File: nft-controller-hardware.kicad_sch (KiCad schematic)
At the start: 24 parts, among them J0 Micro_SD_Card_Det, U0 DS3231M, U1 ADS1115IDGS

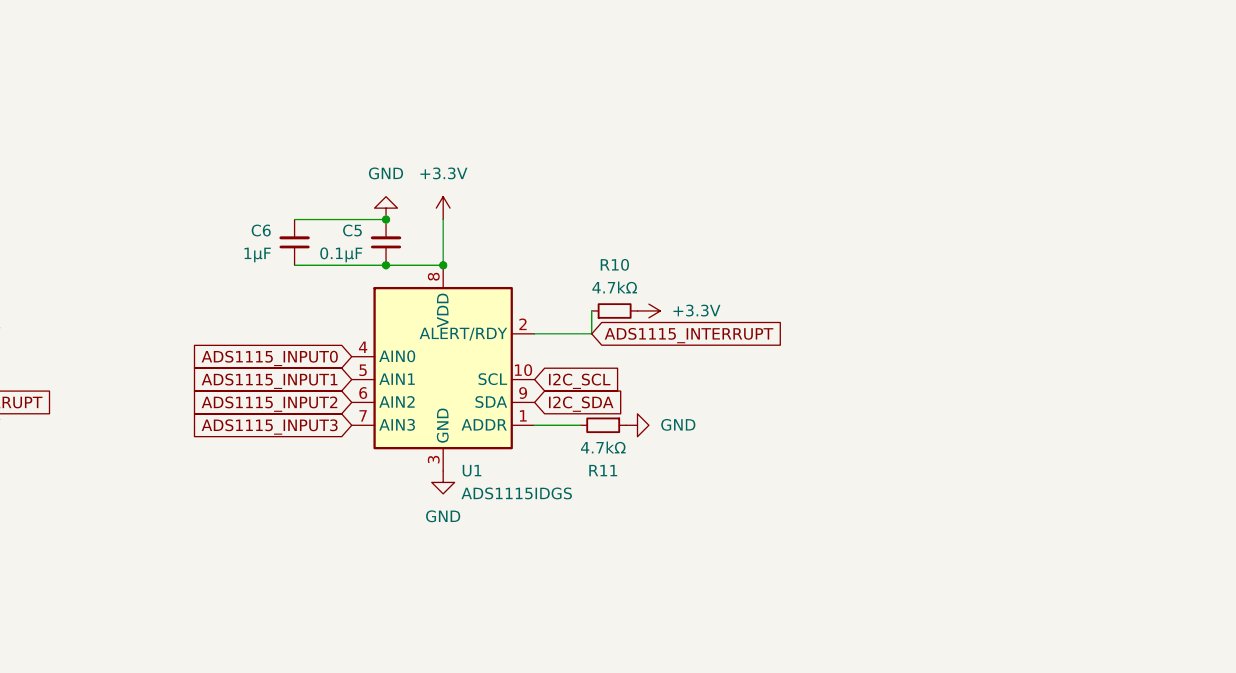
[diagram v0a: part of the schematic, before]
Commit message: Add ADC connectors to the memory expansion board.
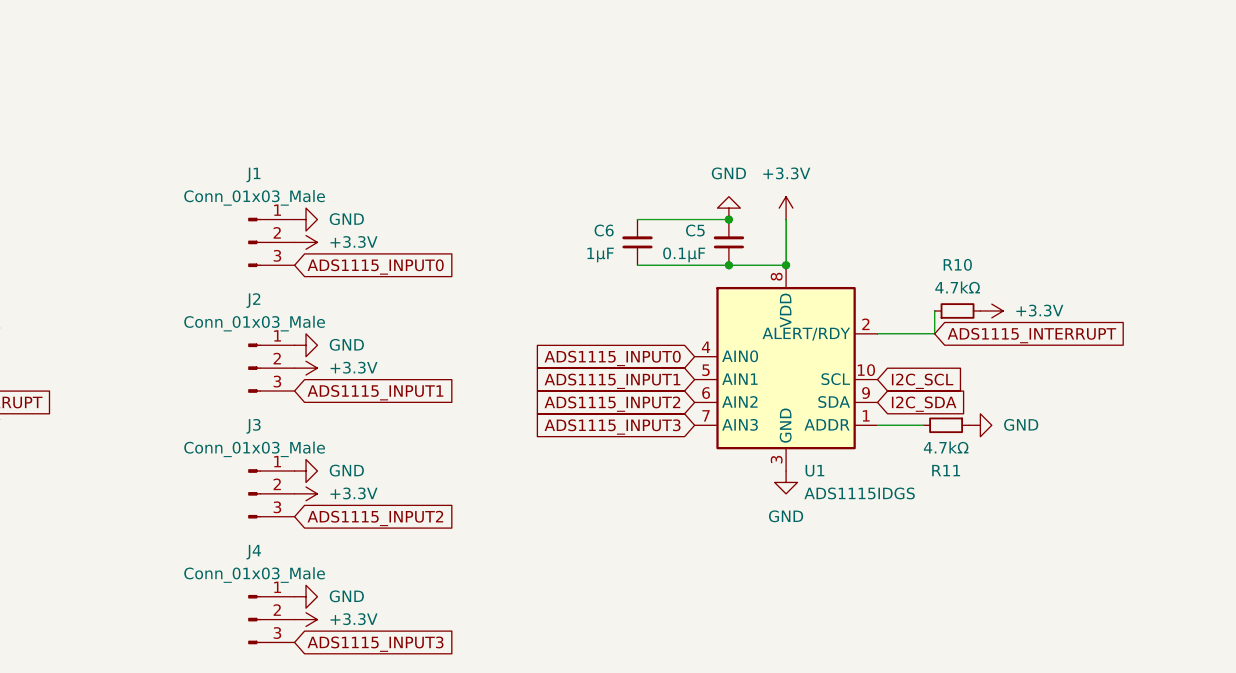
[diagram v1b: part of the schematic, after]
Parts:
- added J1, J2, J3, J4: Conn_01x03_Male, Connector_JST:JST_SH_SM03B-SRSS-TB_1x03-1MP_P1.00mm_Horizontal, symbol Connector:Conn_01x03_Male
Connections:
- net +3V3: now also J1.2 (Pin_2), J2.2 (Pin_2), J3.2 (Pin_2), J4.2 (Pin_2)
- net ADS1115_INPUT0: now also J1.3 (Pin_3)
- net ADS1115_INPUT1: now also J2.3 (Pin_3)
- net ADS1115_INPUT2: now also J3.3 (Pin_3)
- net ADS1115_INPUT3: now also J4.3 (Pin_3)
- net GND: now also J1.1 (Pin_1), J2.1 (Pin_1), J3.1 (Pin_1), J4.1 (Pin_1)
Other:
- moved on the sheet: C5, C6, R10, R11, U1

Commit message: Size all SMD capacitors to 2012.
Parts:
- C0, C1, C2, C3, C4, C5, C6: footprint (none) -> Capacitor_SMD:C_0805_2012Metric
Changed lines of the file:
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@@
       (effects (font (size 1.27 1.27)) (justify right))
     )
-    (property "Footprint" "" (id 2) (at 144.78 124.46 0)
+    (property "Footprint" "Capacitor_SMD:C_0805_2012Metric" (id 2) (at 144.78 124.46 0)
       (effects (font (size 1.27 1.27)) hide)
     )
@@
     (property "Reference" "C2" (id 0) (at 114.2937 67.31 90))
     (property "Value" "1μF" (id 1) (at 114.2937 64.77 90))
-    (property "Footprint" "" (id 2) (at 114.3 60.96 0)
+    (property "Footprint" "Capacitor_SMD:C_0805_2012Metric" (id 2) (at 114.3 60.96 0)
       (effects (font (size 1.27 1.27)) hide)
     )
@@
       (effects (font (size 1.27 1.27)) (justify right))
     )
-    (property "Footprint" "" (id 2) (at 45.72 27.94 0)
+    (property "Footprint" "Capacitor_SMD:C_0805_2012Metric" (id 2) (at 45.72 27.94 0)
       (effects (font (size 1.27 1.27)) hide)
     )
@@
       (effects (font (size 1.27 1.27)) (justify right))
     )
-    (property "Footprint" "" (id 2) (at 154.94 124.46 0)
+    (property "Footprint" "Capacitor_SMD:C_0805_2012Metric" (id 2) (at 154.94 124.46 0)
       (effects (font (size 1.27 1.27)) hide)
     )
@@
       (effects (font (size 1.27 1.27)) (justify left))
     )
-    (property "Footprint" "" (id 2) (at 35.56 127 0)
+    (property "Footprint" "Capacitor_SMD:C_0805_2012Metric" (id 2) (at 35.56 127 0)
       (effects (font (size 1.27 1.27)) hide)
     )
@@
     (property "Reference" "C1" (id 0) (at 114.2937 57.15 90))
     (property "Value" "0.1μF" (id 1) (at 114.2937 54.61 90))
-    (property "Footprint" "" (id 2) (at 114.3 50.8 0)
+    (property "Footprint" "Capacitor_SMD:C_0805_2012Metric" (id 2) (at 114.3 50.8 0)
       (effects (font (size 1.27 1.27)) hide)
     )
@@
       (effects (font (size 1.27 1.27)) (justify left))
     )
-    (property "Footprint" "" (id 2) (at 25.4 127 0)
+    (property "Footprint" "Capacitor_SMD:C_0805_2012Metric" (id 2) (at 25.4 127 0)
       (effects (font (size 1.27 1.27)) hide)
     )
@@
     )
     (path "/2d1d279f-dfe4-4ca3-b77e-718d321d7994"
-      (reference "C0") (unit 1) (value "10μF") (footprint "")
+      (reference "C0") (unit 1) (value "10μF") (footprint "Capacitor_SMD:C_0805_2012Metric")
     )
     (path "/eeddbc36-f79b-450c-949d-4075e2ee2f66"
-      (reference "C1") (unit 1) (value "0.1μF") (footprint "")
+      (reference "C1") (unit 1) (value "0.1μF") (footprint "Capacitor_SMD:C_0805_2012Metric")
     )
     (path "/24f11e55-c826-4157-a61d-34245686f7ab"
-      (reference "C2") (unit 1) (value "1μF") (footprint "")
+      (reference "C2") (unit 1) (value "1μF") (footprint "Capacitor_SMD:C_0805_2012Metric")
     )
     (path "/d8c4663a-d59c-454a-82f0-37282ddac6f7"
-      (reference "C3") (unit 1) (value "0.1μF") (footprint "")
+      (reference "C3") (unit 1) (value "0.1μF") (footprint "Capacitor_SMD:C_0805_2012Metric")
     )
     (path "/f49fb1be-539b-44b6-83f7-76b29af6c384"
-      (reference "C4") (unit 1) (value "1μF") (footprint "")
+      (reference "C4") (unit 1) (value "1μF") (footprint "Capacitor_SMD:C_0805_2012Metric")
     )
     (path "/5a402334-f447-450e-a114-56a61e72962d"
-      (reference "C5") (unit 1) (value "0.1μF") (footprint "")
+      (reference "C5") (unit 1) (value "0.1μF") (footprint "Capacitor_SMD:C_0805_2012Metric")
     )
     (path "/02bbd9ce-68b0-4271-9eb1-4b98656ac324"
-      (reference "C6") (unit 1) (value "1μF") (footprint "")
+      (reference "C6") (unit 1) (value "1μF") (footprint "Capacitor_SMD:C_0805_2012Metric")
     )
     (path "/178ea558-ba01-4660-95f1-80290a5a4f0c"

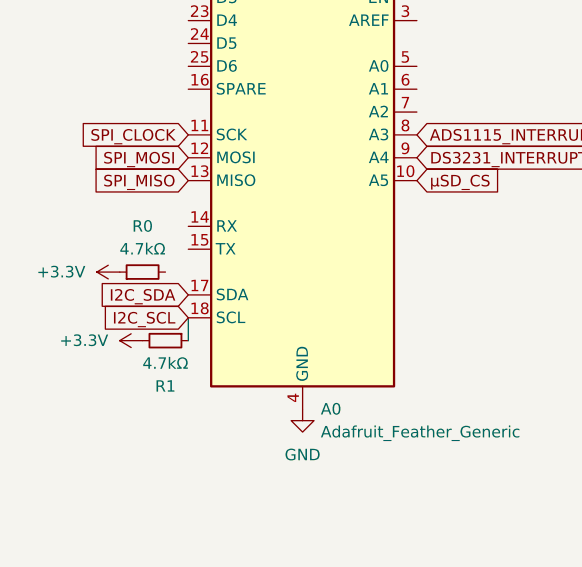
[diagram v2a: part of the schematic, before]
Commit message: Fix a missing connection to an I2C SDA pull-up resistor.
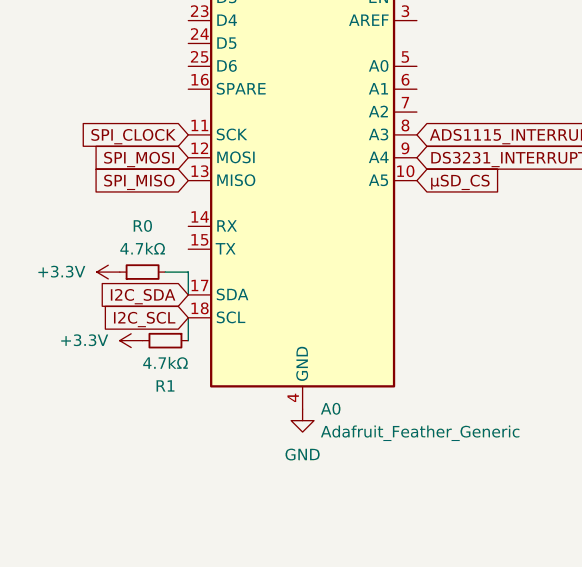
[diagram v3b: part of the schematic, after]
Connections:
- net I2C_SDA: now also R0.2
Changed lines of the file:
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@@
+    (stroke (width 0) (type default) (color 0 0 0 0))
+  )
+  (wire (pts (xy 36.83 81.28) (xy 34.29 81.28))
     (stroke (width 0) (type default) (color 0 0 0 0))
   )
@@
     (stroke (width 0) (type default) (color 0 0 0 0))
   )
+  (wire (pts (xy 36.83 83.82) (xy 36.83 81.28))
+    (stroke (width 0) (type default) (color 0 0 0 0))
+  )
